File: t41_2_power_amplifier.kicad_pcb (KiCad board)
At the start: 2 copper layers, 100 x 100 mm, 61 parts, among them J1 5-1814832-1, J2 5-1814832-1, J3 B2B-XH-A_LF__SN_, J5 Screw_Terminal_01x02, Q1 Q_NMOS_GSD, Q2 Q_NPN_BCE, Q3 Q_NMOS_GSD, Q4 Q_NPN_BCE, Q5 PMOS, Q6 Q_NPN_BCE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

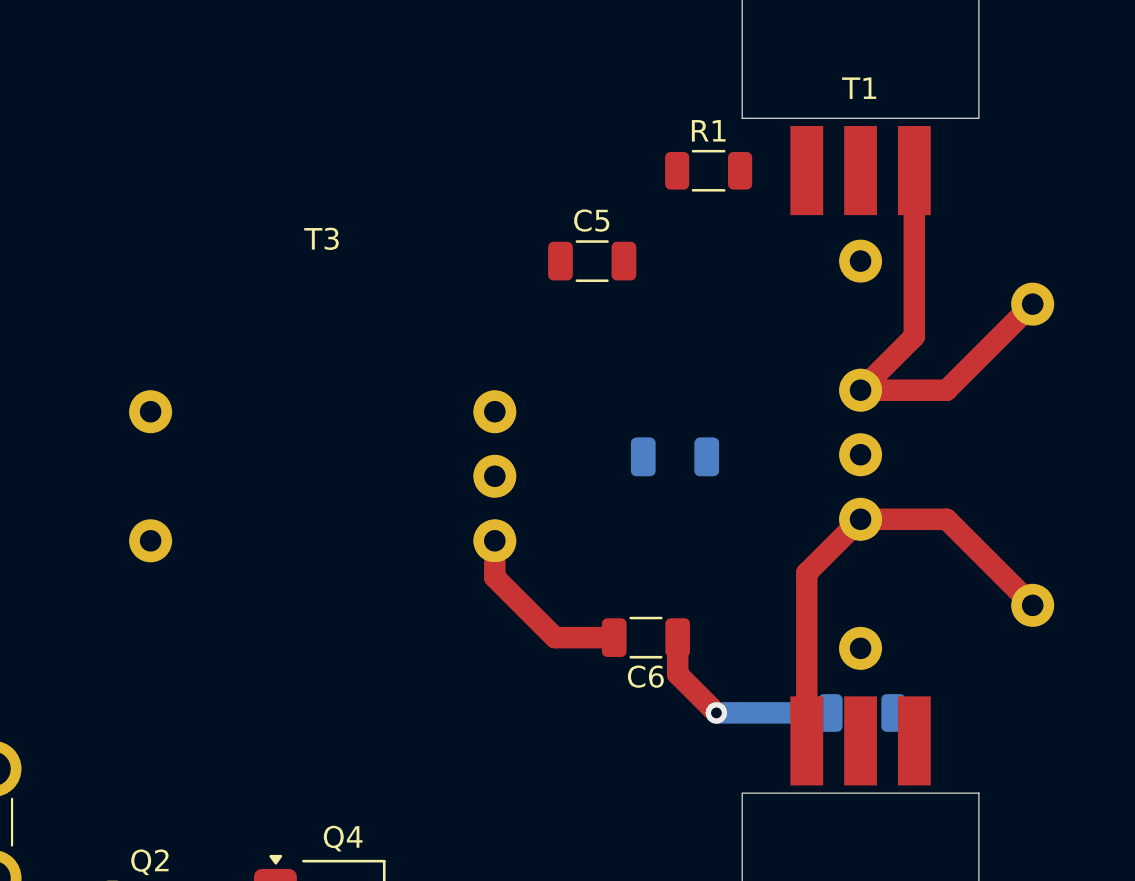
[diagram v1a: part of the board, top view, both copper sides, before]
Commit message: Branching to no-feedback experiment.
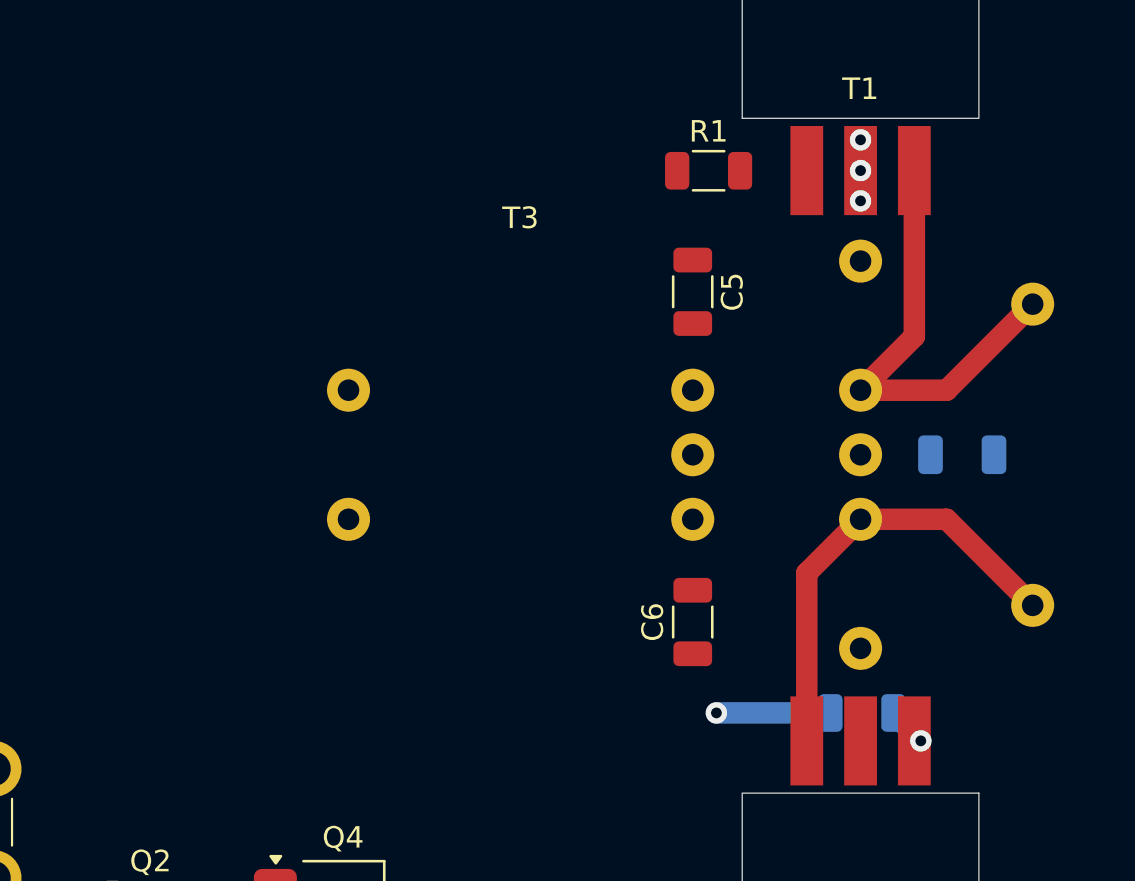
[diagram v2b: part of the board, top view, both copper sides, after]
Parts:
- moved C1 13.4 mm to (155.7, 90.0)
- moved T3 9.25 mm to (135.2, 90.0)
- moved C5 4.89 mm to (143.2, 82.4), turned to -90 degrees
- moved C6 2.29 mm to (143.2, 97.8), turned to 90 degrees
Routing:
- net Net-(T3-SA): track 8.41 -> 0.00 mm
- net Net-(C6-Pad1): track 9.55 -> 5.30 mm
- net GND: track 0.00 -> 2.84 mm, vias 0 -> 3
- net Net-(Q1-G): track 0.00 -> 2.33 mm, vias 0 -> 1
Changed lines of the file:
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@@
 		(allow_soldermask_bridges_in_footprints no)
 		(pcbplotparams
-			(layerselection 0x00010fc_ffffffff)
+			(layerselection 0x00010f0_ffffffff)
 			(plot_on_all_layers_selection 0x0000000_00000000)
 			(disableapertmacros no)
@@
 			(usegerberattributes yes)
 			(usegerberadvancedattributes yes)
-			(creategerberjobfile yes)
+			(creategerberjobfile no)
 			(dashed_line_dash_ratio 12.000000)
 			(dashed_line_gap_ratio 3.000000)
@@
 			(outputformat 1)
 			(mirror no)
-			(drillshape 1)
+			(drillshape 0)
 			(scaleselection 1)
-			(outputdirectory "")
+			(outputdirectory "gerber/")
 		)
 	)
@@
 	(footprint "Capacitor_SMD:C_1206_3216Metric"
 		(layer "F.Cu")
-		(at 141.025 98.5 180)
+		(at 143.2 97.775 90)
 		(descr "Capacitor SMD 1206 (3216 Metric), square (rectangular) end terminal, IPC_7351 nominal, (Body size source: IPC-SM-782 page 76, https://www.pcb-3d.com/wordpress/wp-content/uploads/ipc-sm-782a_amendment_1_and_2.pdf), generated with kicad-footprint-generator")
 		(tags "capacitor")
 		(property "Reference" "C6"
-			(at 0 -1.85 360)
+			(at 0 -1.85 90)
 			(layer "F.SilkS")
 			(effects
@@
 		)
 		(property "Value" "0.1uF"
-			(at 0 1.85 360)
+			(at 0 1.85 90)
 			(layer "F.Fab")
 			(effects
@@
 		)
 		(property "Footprint" "Capacitor_SMD:C_1206_3216Metric"
-			(at 0 0 180)
+			(at 0 0 90)
 			(unlocked yes)
 			(layer "F.Fab")
@@
 		)
 		(property "Datasheet" ""
-			(at 0 0 180)
+			(at 0 0 90)
 			(unlocked yes)
 			(layer "F.Fab")
@@
 		)
 		(property "Description" "Unpolarized capacitor, small symbol"
-			(at 0 0 180)
+			(at 0 0 90)
 			(unlocked yes)
 			(layer "F.Fab")
@@
 		(attr smd)
 		(fp_line
-			(start -0.711252 0.91)
-			(end 0.711252 0.91)
+			(start -0.711252 -0.91)
+			(end 0.711252 -0.91)
 			(stroke
 				(width 0.12)
@@
 		)
 		(fp_line
-			(start -0.711252 -0.91)
-			(end 0.711252 -0.91)
+			(start -0.711252 0.91)
+			(end 0.711252 0.91)
 			(stroke
 				(width 0.12)
@@
 		)
 		(fp_line
-			(start 2.3 1.15)
-			(end -2.3 1.15)
+			(start 2.3 -1.15)
+			(end 2.3 1.15)
 			(stroke
 				(width 0.05)
@@
 		)
 		(fp_line
-			(start 2.3 -1.15)
-			(end 2.3 1.15)
+			(start -2.3 -1.15)
+			(end 2.3 -1.15)
 			(stroke
 				(width 0.05)
@@
 		)
 		(fp_line
-			(start -2.3 1.15)
-			(end -2.3 -1.15)
+			(start 2.3 1.15)
+			(end -2.3 1.15)
 			(stroke
 				(width 0.05)
@@
 		)
 		(fp_line
-			(start -2.3 -1.15)
-			(end 2.3 -1.15)
+			(start -2.3 1.15)
+			(end -2.3 -1.15)
 			(stroke
 				(width 0.05)
@@
 		)
 		(fp_line
-			(start 1.6 0.8)
-			(end -1.6 0.8)
+			(start 1.6 -0.8)
+			(end 1.6 0.8)
 			(stroke
 				(width 0.1)
@@
 		)
 		(fp_line
-			(start 1.6 -0.8)
-			(end 1.6 0.8)
+			(start -1.6 -0.8)
+			(end 1.6 -0.8)
 			(stroke
 				(width 0.1)
@@
 		)
 		(fp_line
-			(start -1.6 0.8)
-			(end -1.6 -0.8)
+			(start 1.6 0.8)
+			(end -1.6 0.8)
 			(stroke
 				(width 0.1)
@@
 		)
 		(fp_line
-			(start -1.6 -0.8)
-			(end 1.6 -0.8)
+			(start -1.6 0.8)
+			(end -1.6 -0.8)
 			(stroke
 				(width 0.1)
@@
 		)
 		(fp_text user "${REFERENCE}"
-			(at 0 0 360)
+			(at 0 0 90)
 			(layer "F.Fab")
 			(effects
@@
 		)
 		(pad "1" smd roundrect
-			(at -1.475 0 180)
+			(at -1.475 0 90)
 			(size 1.15 1.8)
 			(layers "F.Cu" "F.Paste" "F.Mask")
@@
 		)
 		(pad "2" smd roundrect
-			(at 1.475 0 180)
+			(at 1.475 0 90)
 			(size 1.15 1.8)
 			(layers "F.Cu" "F.Paste" "F.Mask")
@@
 	(footprint "Binocular_Core:BN-43-302"
 		(layer "F.Cu")
-		(at 126 91)
+		(at 135.2 90)
 		(property "Reference" "T3"
 			(at 0 -11 0)
@@
 	(footprint "Capacitor_SMD:C_1206_3216Metric"
 		(layer "F.Cu")
-		(at 138.525 81)
+		(at 143.2 82.425 -90)
 		(descr "Capacitor SMD 1206 (3216 Metric), square (rectangular) end terminal, IPC_7351 nominal, (Body size source: IPC-SM-782 page 76, https://www.pcb-3d.com/wordpress/wp-content/uploads/ipc-sm-782a_amendment_1_and_2.pdf), generated with kicad-footprint-generator")
 		(tags "capacitor")
 		(property "Reference" "C5"
-			(at 0 -1.85 0)
+			(at 0 -1.85 90)
 			(layer "F.SilkS")
 			(effects
@@
 		)
 		(property "Value" "0.1uF"
-			(at 0 1.85 0)
+			(at 0 1.85 90)
 			(layer "F.Fab")
 			(effects
@@
 		)
 		(property "Footprint" "Capacitor_SMD:C_1206_3216Metric"
-			(at 0 0 0)
+			(at 0 0 -90)
 			(unlocked yes)
 			(layer "F.Fab")
@@
 		)
 		(property "Datasheet" ""
-			(at 0 0 0)
+			(at 0 0 -90)
 			(unlocked yes)
 			(layer "F.Fab")
@@
 		)
 		(property "Description" "Unpolarized capacitor, small symbol"
-			(at 0 0 0)
+			(at 0 0 -90)
 			(unlocked yes)
 			(layer "F.Fab")
@@
 		(attr smd)
 		(fp_line
-			(start -0.711252 -0.91)
-			(end 0.711252 -0.91)
+			(start -0.711252 0.91)
+			(end 0.711252 0.91)
 			(stroke
 				(width 0.12)
@@
 		)
 		(fp_line
-			(start -0.711252 0.91)
-			(end 0.711252 0.91)
+			(start -0.711252 -0.91)
+			(end 0.711252 -0.91)
 			(stroke
 				(width 0.12)
@@
 		)
 		(fp_line
-			(start -2.3 -1.15)
-			(end 2.3 -1.15)
+			(start -2.3 1.15)
+			(end -2.3 -1.15)
 			(stroke
 				(width 0.05)
@@
 		)
 		(fp_line
-			(start -2.3 1.15)
-			(end -2.3 -1.15)
+			(start 2.3 1.15)
+			(end -2.3 1.15)
 			(stroke
 				(width 0.05)
@@
 		)
 		(fp_line
-			(start 2.3 -1.15)
-			(end 2.3 1.15)
+			(start -2.3 -1.15)
+			(end 2.3 -1.15)
 			(stroke
 				(width 0.05)
@@
 		)
 		(fp_line
-			(start 2.3 1.15)
-			(end -2.3 1.15)
+			(start 2.3 -1.15)
+			(end 2.3 1.15)
 			(stroke
 				(width 0.05)
@@
 		)
 		(fp_line
-			(start -1.6 -0.8)
-			(end 1.6 -0.8)
+			(start -1.6 0.8)
+			(end -1.6 -0.8)
 			(stroke
 				(width 0.1)
@@
 		)
 		(fp_line
-			(start -1.6 0.8)
-			(end -1.6 -0.8)
+			(start 1.6 0.8)
+			(end -1.6 0.8)
 			(stroke
 				(width 0.1)
@@
 		)
 		(fp_line
-			(start 1.6 -0.8)
-			(end 1.6 0.8)
+			(start -1.6 -0.8)
+			(end 1.6 -0.8)
 			(stroke
 				(width 0.1)
@@
 		)
 		(fp_line
-			(start 1.6 0.8)
-			(end -1.6 0.8)
+			(start 1.6 -0.8)
+			(end 1.6 0.8)
 			(stroke
 				(width 0.1)
@@
 		)
 		(fp_text user "${REFERENCE}"
-			(at 0 0 0)
+			(at 0 0 90)
 			(layer "F.Fab")
 			(effects
@@
 		)
 		(pad "1" smd roundrect
-			(at -1.475 0)
+			(at -1.475 0 270)
 			(size 1.15 1.8)
 			(layers "F.Cu" "F.Paste" "F.Mask")
@@
 		)
 		(pad "2" smd roundrect
-			(at 1.475 0)
+			(at 1.475 0 270)
 			(size 1.15 1.8)
 			(layers "F.Cu" "F.Paste" "F.Mask")
@@
 	(footprint "Capacitor_SMD:C_1206_3216Metric"
 		(layer "B.Cu")
-		(at 142.375 90.1)
+		(at 155.725 90)
 		(descr "Capacitor SMD 1206 (3216 Metric), square (rectangular) end terminal, IPC_7351 nominal, (Body size source: IPC-SM-782 page 76, https://www.pcb-3d.com/wordpress/wp-content/uploads/ipc-sm-782a_amendment_1_and_2.pdf), generated with kicad-footprint-generator")
 		(tags "capacitor")
@@
 		(tags "resistor")
 		(property "Reference" "R2"
-			(at 0 1.82 360)
+			(at 0 1.82 0)
 			(layer "B.SilkS")
 			(effects
@@
 		)
 		(property "Value" "1"
-			(at 0 -1.82 360)
+			(at 0 -1.82 0)
 			(layer "B.Fab")
 			(effects
@@
 		)
 		(fp_text user "${REFERENCE}"
-			(at 0 0 360)
+			(at 0 0 0)
 			(layer "B.Fab")
 			(effects
@@
 	)
 	(segment
+		(start 151 76.791)
+		(end 151 75.3625)
+		(width 0.2)
+		(layer "F.Cu")
+		(net 2)
+	)
+	(segment
+		(start 151 76.791)
+		(end 151 78.2)
+		(width 0.2)
+		(layer "F.Cu")
+		(net 2)
+	)
+	(via
+		(at 151 78.2)
+		(size 1)
+		(drill 0.5)
+		(layers "F.Cu" "B.Cu")
+		(net 2)
+	)
+	(via
+		(at 151 75.3625)
+		(size 1)
+		(drill 0.5)
+		(layers "F.Cu" "B.Cu")
+		(net 2)
+	)
+	(via
+		(at 151 76.791)
+		(size 1)
+		(drill 0.5)
+		(layers "F.Cu" "B.Cu")
+		(net 2)
+	)
+	(segment
 		(start 153.5 76.791)
 		(end 153.5 84.5)
@@
 		(net 4)
 	)
-	(segment
-		(start 134 94)
-		(end 134 95.7)
-		(width 1)
-		(layer "F.Cu")
-		(net 11)
-	)
-	(segment
-		(start 136.8 98.5)
-		(end 139.55 98.5)
-		(width 1)
-		(layer "F.Cu")
-		(net 11)
-	)
-	(segment
-		(start 134 95.7)
-		(end 136.8 98.5)
-		(width 1)
-		(layer "F.Cu")
-		(net 11)
+	(via
+		(at 144.3 102)
+		(size 1)
+		(drill 0.5)
+		(layers "F.Cu" "B.Cu")
+		(net 12)
 	)
 	(segment
-		(start 142.5 98.5)
-		(end 142.5 100.2)
+		(start 144.3 102)
+		(end 149.6 102)
 		(width 1)
-		(layer "F.Cu")
+		(layer "B.Cu")
 		(net 12)
 	)
 	(segment
-		(start 142.5 100.2)
-		(end 144.3 102)
-		(width 1)
+		(start 153.5 103.3)
+		(end 154 103.3)
+		(width 0.2)
 		(layer "F.Cu")
-		(net 12)
+		(net 30)
 	)
 	(via
-		(at 144.3 102)
+		(at 153.8 103.3)
 		(size 1)
 		(drill 0.5)
 		(layers "F.Cu" "B.Cu")
-		(net 12)
+		(net 30)
 	)
 	(segment
-		(start 144.3 102)
-		(end 149.6 102)
+		(start 152.525 102)
+		(end 152.525 102.025)
 		(width 1)
 		(layer "B.Cu")
-		(net 12)
+		(net 30)
+	)
+	(segment
+		(start 152.525 102.025)
+		(end 153.8 103.3)
+		(width 1)
+		(layer "B.Cu")
+		(net 30)
 	)
 	(zone

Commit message: Finishing PCB placement.  Stopping point.
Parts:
- removed C4: 0.1uF, Capacitor_SMD:C_1206_3216Metric
- removed R3, R4: DNP, Resistor_SMD:R_1206_3216Metric
- removed T1: Transformer_1P_SS, Binocular_Core:BN-43-202_VERTICAL
- added L2: ~, Binocular_Core:BN-43-202_VERTICAL, F.Cu at (151.0, 90.0)
- C2: value 180pF -> 100pF
- C3: value 0.1uF -> 100pF
- R14: value 56 -> 1000
- moved C11 164.3 mm to (189.6, 141.3), turned to 180 degrees
- moved C14 159.2 mm to (194.7, 128.5), turned to 180 degrees
- moved C18 154.5 mm to (194.6, 123.5), turned to 180 degrees
- moved C13 153.8 mm to (180.6, 142.7), turned to 180 degrees
- moved C12 129.3 mm to (154.9, 134.6), turned to -90 degrees
- moved C3 124.3 mm to (161.4, 90.0), turned to -90 degrees
- moved C2 122.3 mm to (158.4, 90.0), turned to -90 degrees
- moved R19 111.4 mm to (127.9, 126.0)
- moved R20 110.0 mm to (141.1, 118.4), turned to 180 degrees
- moved C7 106.8 mm to (136.4, 111.7), turned to 180 degrees
- moved R5 99.0 mm to (137.5, 98.5)
- moved R6 99.0 mm to (137.5, 101.8)
- moved R16 94.8 mm to (116.3, 107.0), turned to 180 degrees
- moved R18 87.4 mm to (114.8, 102.7), turned to 90 degrees
- moved C19 87.4 mm to (122.3, 119.5), turned to 180 degrees
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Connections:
- C3 pad 1: Net-(C3-Pad1) -> Net-(Q3-D)
- C3 pad 2: Net-(T1-AA) -> Net-(Q1-D)
- Q4 pad 1: Net-(Q2-E) -> Net-(Q4-E)
- Q4 pad 2: Net-(Q2-C) -> Net-(Q2-E)
- Q4 pad 4: (no net) -> Net-(Q2-C)
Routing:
- net Net-(Q4-E): track 0.00 -> 10.8 mm
- net Net-(Q3-G): track 0.00 -> 5.91 mm
- net GND: track 2.84 -> 7.60 mm, vias 3 -> 6
- net Net-(Q1-G): track 2.33 -> 6.60 mm
- net Net-(C5-Pad1): track 0.00 -> 3.83 mm
- net Net-(T3-SA): track 0.00 -> 3.30 mm
- net /12V_OUT_FIL: track 0.00 -> 3.25 mm
- net Net-(Q3-D): track 20.9 -> 17.7 mm
- net Net-(T3-SB): track 0.00 -> 3.10 mm
- net Net-(Q2-E): track 0.00 -> 2.25 mm, vias 0 -> 1
- net Net-(C6-Pad1): track 5.30 -> 7.39 mm
- net Net-(Q1-D): track 21.0 -> 22.4 mm
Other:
- outline, holes or cut-outs redrawn
- board text added: "KF5N"
- board text added: "T41-2 POWER AMPLIFIER"

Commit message: Routed.  Needs cleanup.
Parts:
- removed C19: 0.1uF, Capacitor_SMD:C_1206_3216Metric
- added C20: 1uf, Capacitor_SMD:C_1206_3216Metric, F.Cu at (141.8, 123.7)
- added C4: 0.1uF, Capacitor_SMD:C_1206_3216Metric, B.Cu at (154.7, 93.0)
- E4, E5: value 28F0121-0SR-10 -> XXX; footprint 28F0121_0SR_10:FB_28F0121-0SR-10 -> Inductor_SMD:L_1206_3216Metric
- Q5: value PMOS -> Q_PMOS_GSD; footprint Package_TO_SOT_SMD:SOT-23 -> Package_TO_SOT_SMD:SOT-23-3
- Q6: value Q_NPN_BCE -> Q_NPN_BEC; footprint Package_TO_SOT_SMD:SOT-23 -> Package_TO_SOT_SMD:SOT-23-3
- moved C11 76.7 mm to (115.7, 120.8), turned to 90 degrees
- moved E4 75.4 mm to (114.1, 116.5)
- moved U1 53.4 mm to (144.2, 119.7), turned to 90 degrees
- moved C14 51.7 mm to (144.7, 115.3), turned to 0 degrees
- moved C18 51.2 mm to (144.7, 112.0), turned to 0 degrees
- moved J2 39.9 mm to (105.9, 67.3)
- moved R16 38.6 mm to (112.5, 68.7), turned to 90 degrees
- moved R15 36.4 mm to (122.0, 65.0)
- moved R18 34.6 mm to (116.7, 68.2), turned to 0 degrees
- moved Q6 33.9 mm to (117.8, 102.9), turned to 90 degrees
- moved E5 33.1 mm to (136.0, 120.9), turned to 180 degrees
- moved C15 32.3 mm to (122.0, 68.2), turned to 180 degrees
- moved R19 28.4 mm to (119.2, 99.0)
- moved E3 27.0 mm to (157.0, 127.8), turned to 0 degrees
- moved Q5 26.9 mm to (119.3, 95.0), turned to 90 degrees
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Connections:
- Q5 pad 1: /12V_IN_FIL -> Net-(Q5-G)
- Q5 pad 2: Net-(Q5-G) -> Net-(Q5-S)
- Q5 pad 3: Net-(Q5-S) -> /12V_IN_FIL
- Q6 pad 2: Net-(Q5-G) -> GND
- Q6 pad 3: GND -> Net-(Q5-G)
- R11 pad 2: Net-(C5-Pad1) -> Net-(C8-Pad2)
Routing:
- net Net-(U1-VIN): track 0.00 -> 60.9 mm
- net /8V: track 0.00 -> 50.1 mm
- net /TXRX: track 0.00 -> 44.4 mm, vias 0 -> 2
- net /12V_OUT_FIL: track 3.25 -> 36.8 mm, vias 0 -> 2
- net Net-(Q5-S): track 0.00 -> 31.6 mm
- net Net-(Q2-C): track 0.00 -> 23.3 mm
- net Net-(D1-K): track 0.00 -> 15.7 mm
- net Net-(T2-SB): track 0.00 -> 15.5 mm
- net Net-(C7-Pad1): track 0.00 -> 11.1 mm
- net Net-(C8-Pad2): track 0.00 -> 11.0 mm
- net Net-(J5-Pin_1): track 0.00 -> 11.0 mm
- net Net-(Q2-E): track 2.25 -> 13.2 mm, vias 1 -> 0
- net Net-(J2-Pad2): track 0.00 -> 9.61 mm
- net /12V_IN_FIL: track 0.00 -> 9.57 mm
- net Net-(Q2-B): track 0.00 -> 8.97 mm
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
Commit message: Almost ready for fab.
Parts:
- R2: moved to F.Cu
- moved E5 20.0 mm to (120.7, 108.0), turned to 90 degrees
- moved C20 10.6 mm to (131.2, 123.7)
- moved C14 10.6 mm to (134.2, 115.4)
- moved C18 10.6 mm to (134.2, 112.0)
- moved U1 10.6 mm to (133.7, 119.8)
- moved R2 4.34 mm to (146.6, 102.0)
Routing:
- net Net-(U1-VIN): track 60.9 -> 83.6 mm
- net Net-(Q5-S): track 31.6 -> 10.4 mm
- net /TXRX: track 44.4 -> 33.9 mm
- net /8V: track 50.1 -> 43.4 mm
- net Net-(Q1-G): track 12.6 -> 17.9 mm, vias 3 -> 6
- net GND: track 7.60 -> 12.7 mm, vias 10 -> 83
- net Net-(C6-Pad1): track 13.3 -> 9.40 mm, vias 1 -> 0
